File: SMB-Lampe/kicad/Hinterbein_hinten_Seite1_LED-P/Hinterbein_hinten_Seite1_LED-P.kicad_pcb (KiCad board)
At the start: 2 copper layers, 7 x 20 mm, 10 parts, among them J1 Conn_01x01_Pin, J2 Conn_01x01_Pin, J3 Conn_01x01_Pin, J4 Conn_01x01_Pin, J5 Conn_01x01_Pin, J6 Conn_01x01_Pin

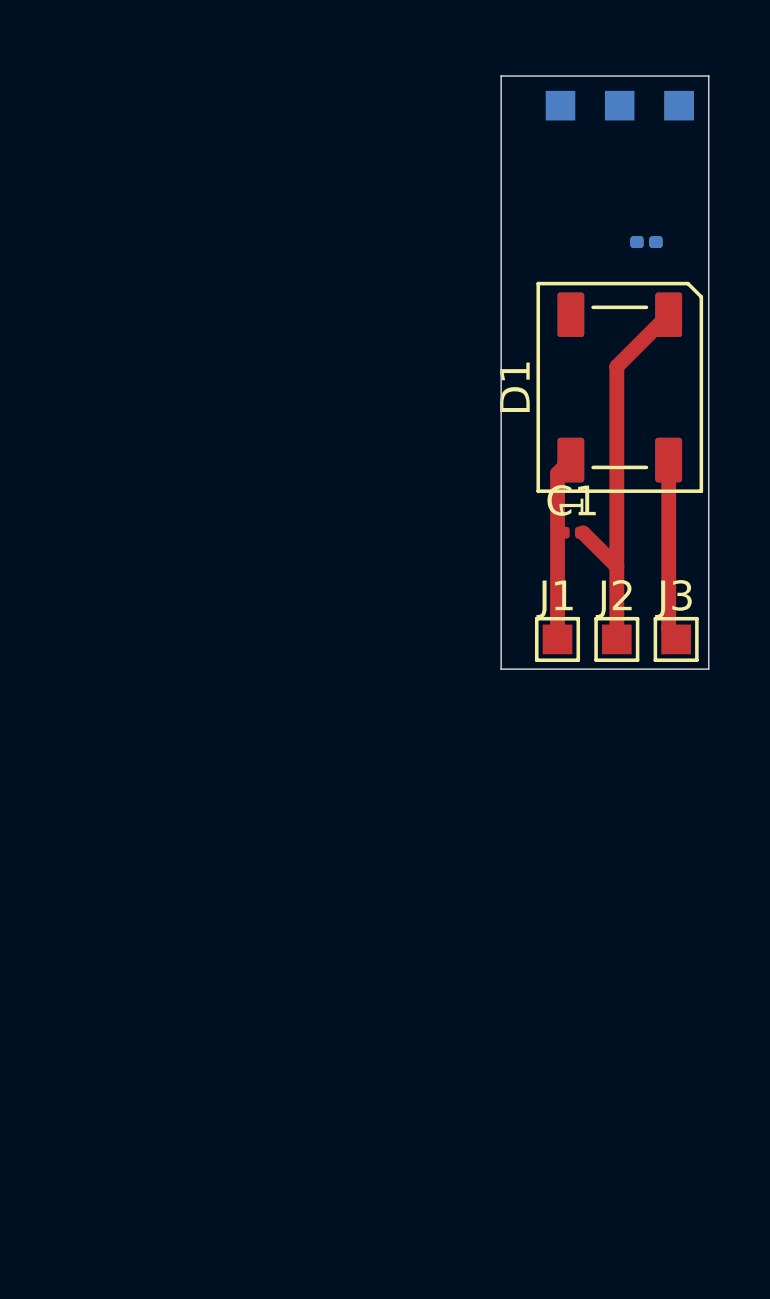
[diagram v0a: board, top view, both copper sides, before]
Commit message: Hinterbein Seite 1/2 erstellt
Anschlüsse zwischen den Platinen mit MountingHoles. Eigenes MountingHole Erstellt
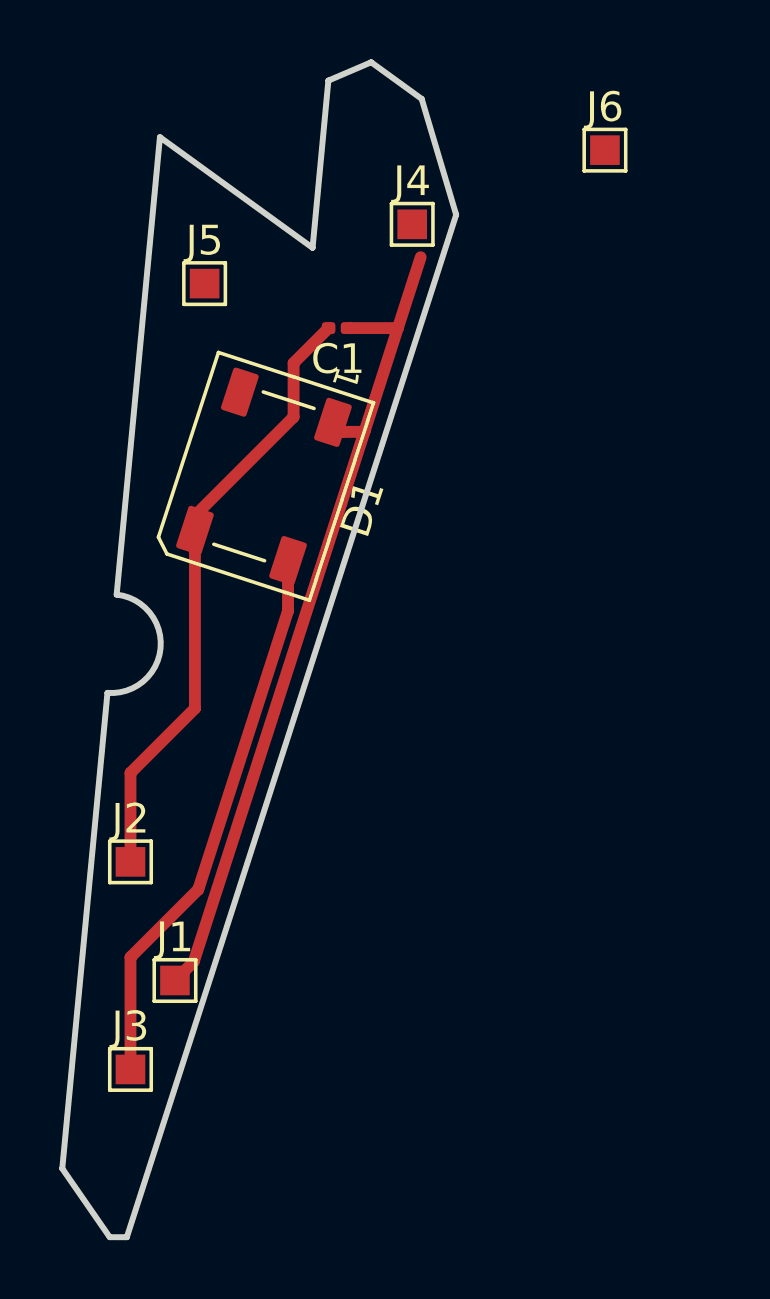
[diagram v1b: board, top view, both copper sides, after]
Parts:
- removed C2: 100nF, Capacitor_SMD:C_0201_0603Metric
- removed D2: WS2812B, LED_SMD:LED_WS2812B_PLCC4_5.0x5.0mm_P3.2mm
- J4, J5, J6: moved to F.Cu
- moved J3 23.4 mm to (127.5, 93.5)
- moved J2 18.0 mm to (127.5, 86.5)
- moved J1 17.3 mm to (129.0, 90.5)
- moved J5 15.2 mm to (130.0, 67.0), turned to 0 degrees
- moved D1 12.4 mm to (132.0, 73.5), turned to -108 degrees
- moved C1 10.5 mm to (134.5, 68.5), turned to 180 degrees
- moved J4 6.40 mm to (137.0, 65.0), turned to 0 degrees
- moved J6 2.92 mm to (143.5, 62.5), turned to 0 degrees
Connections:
- D1 pad 2: /Data_In -> /Data_OUT
- D1 pad 4: Net-(D1-DIN) -> /Data_In
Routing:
- net /+5V: track 6.24 -> 28.7 mm
- net /Data_In: track 6.15 -> 18.6 mm
- net GND: track 13.3 -> 20.8 mm
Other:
- board size 7 x 20 mm -> 13.3 x 39.6 mm
- board text added: "-108°"

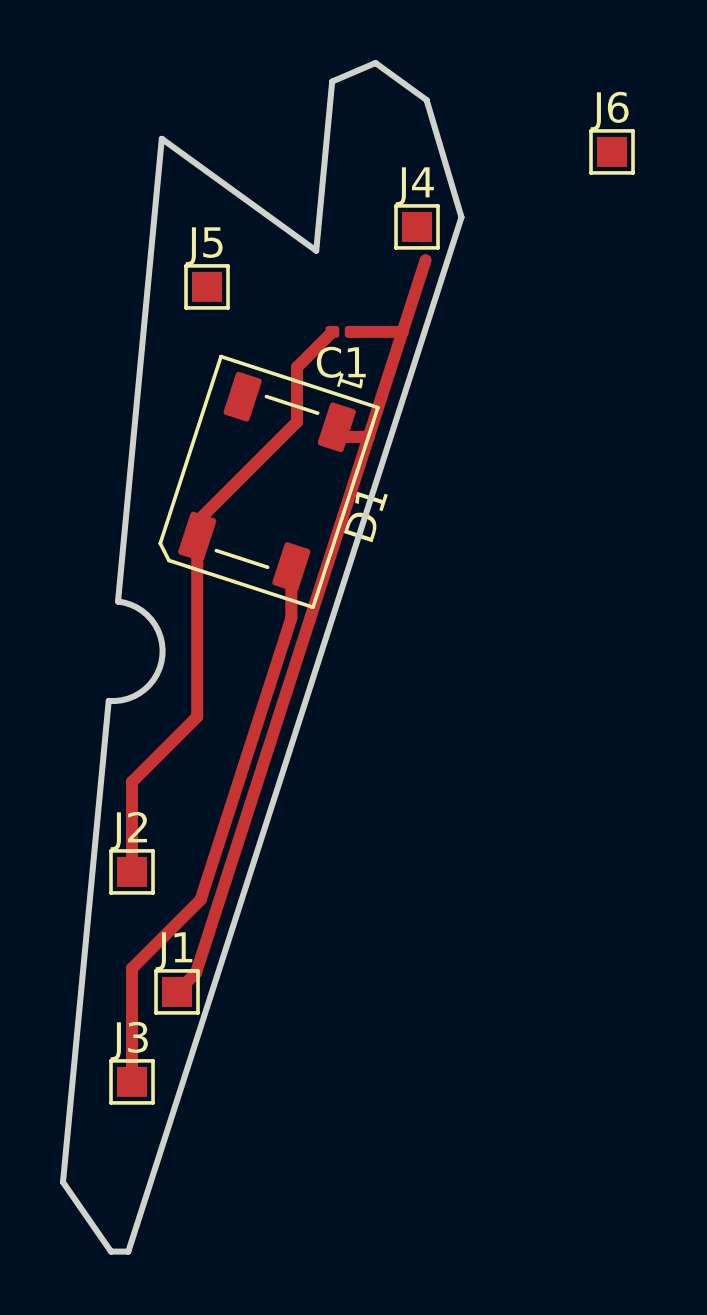
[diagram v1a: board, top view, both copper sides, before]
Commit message: Hinterbein Hinten fertig
Seite 1 und Seite 2 von Hinterbein hinten Sind fertig
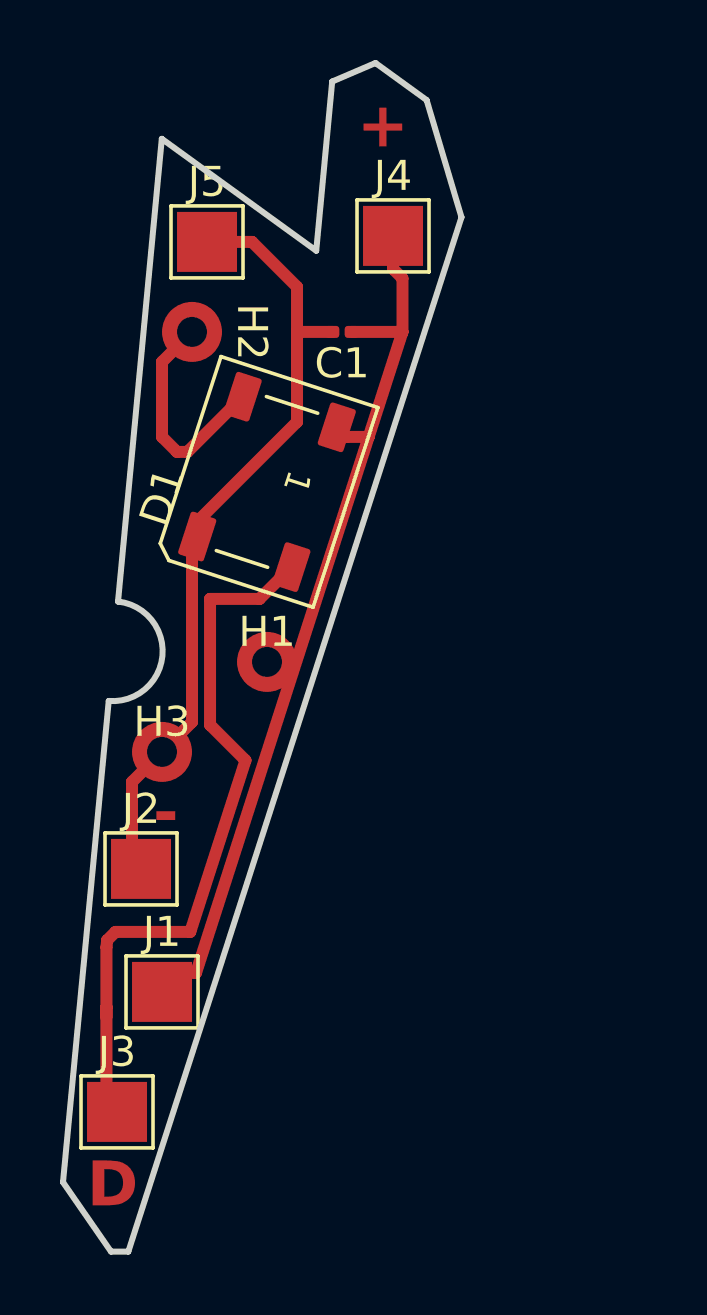
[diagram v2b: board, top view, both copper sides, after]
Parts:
- removed J6: Conn_01x01_Pin, TestPoint:TestPoint_Pad_1.0x1.0mm
- added H1: MountingHole_Pad, Eigenen_Library:MountingHole D2 x d1 test, F.Cu at (132.0, 79.5)
- added H2: MountingHole_Pad, Eigenen_Library:MountingHole D2 x d1 test, F.Cu at (129.5, 68.5)
- added H3: MountingHole_Pad, Eigenen_Library:MountingHole D2 x d1 test, F.Cu at (128.5, 82.5)
- J1, J2, J3, J4, J5: footprint TestPoint:TestPoint_Pad_1.0x1.0mm -> TestPoint:TestPoint_Pad_2.0x2.0mm
- moved J5 1.50 mm to (130.0, 65.5)
- moved J3 1.12 mm to (127.0, 94.5)
- moved J4 0.85 mm to (136.2, 65.3)
- moved J1 0.50 mm to (128.5, 90.5)
- moved J2 0.32 mm to (127.8, 86.4)
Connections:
- net /+5V renamed /+5V_IN_Hauptplatine
- net /Data_In renamed /Data_IN_Hauptplatine
- D1 pad 2: /Data_OUT -> /Data_OUT_Hinterbein_hinten_Seite2
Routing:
- net /Data_OUT_Hinterbein_hinten_Seite2: track 0.00 -> 7.57 mm
- net GND: track 20.8 -> 27.8 mm
- net /Data_IN_Hauptplatine: track 18.6 -> 24.1 mm
- net /+5V_IN_Hauptplatine: track 28.7 -> 30.1 mm
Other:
- board text added: "+"
- board text added: "-"
- board text added: "-108"
- board text added: "D"
- board text removed: "-108°"

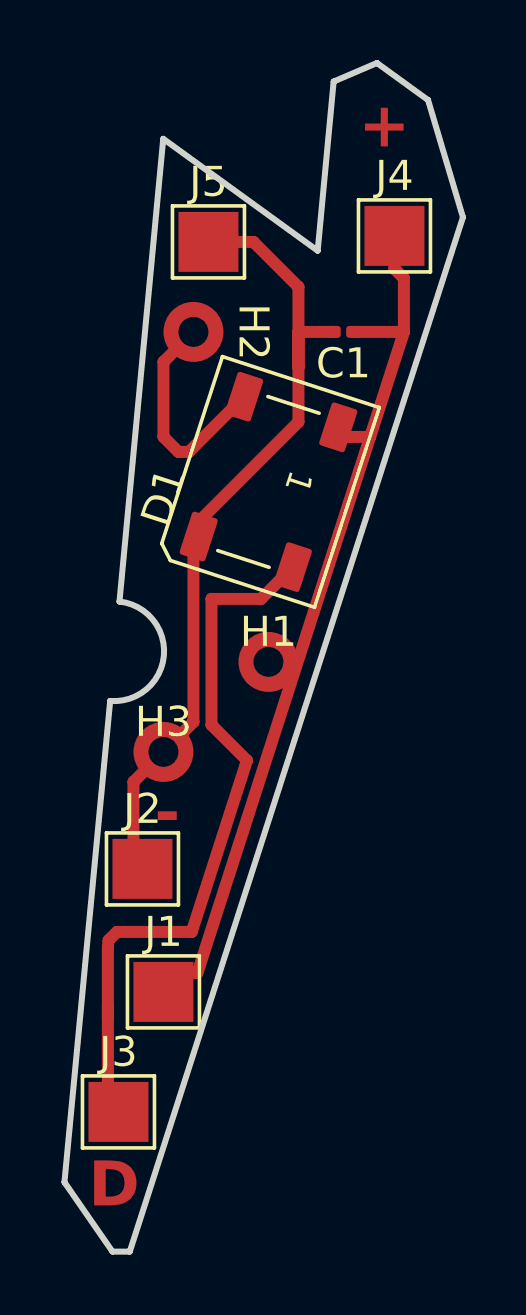
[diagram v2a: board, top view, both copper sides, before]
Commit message: Vorderes Hinterbein fertig
Alle Platinen sind fertig beschaltet
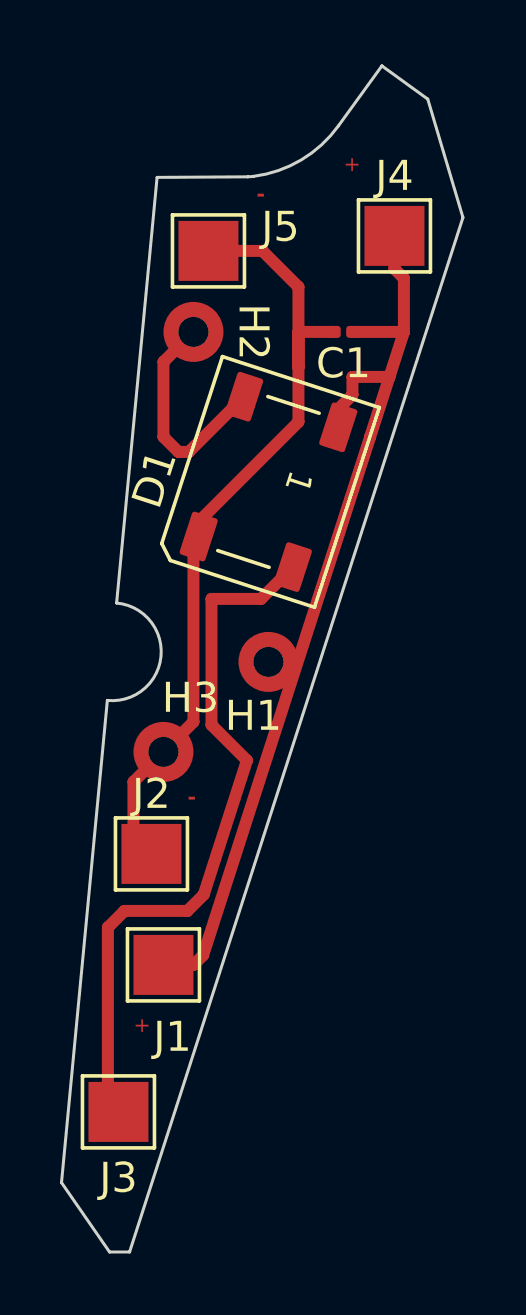
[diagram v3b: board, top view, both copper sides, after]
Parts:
- moved J1 0.90 mm to (128.5, 89.6)
- moved J2 0.58 mm to (128.1, 85.9)
- moved J5 0.30 mm to (130.0, 65.8)
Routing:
- net /+5V_IN_Hauptplatine: track 30.1 -> 31.4 mm
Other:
- board size 13.3 x 39.6 mm -> 13.4 x 39.5 mm
- board text removed: "D"

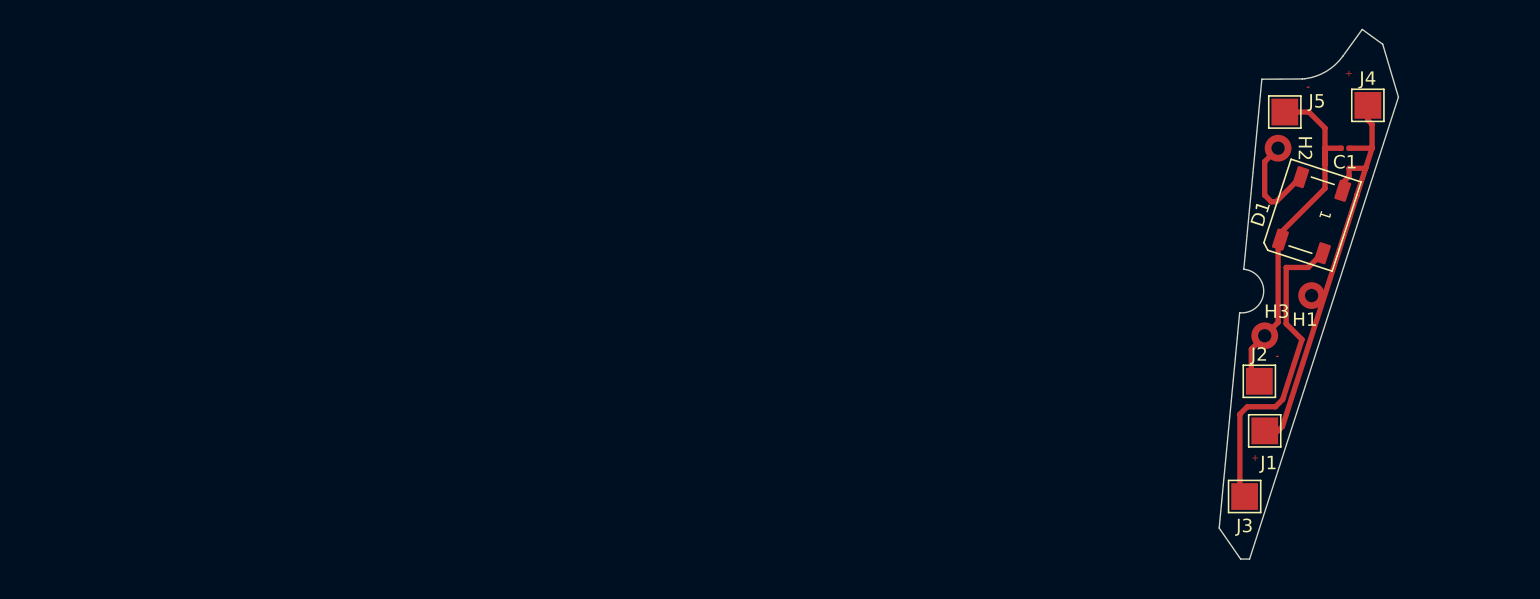
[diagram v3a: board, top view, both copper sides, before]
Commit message: Hinterbeine Geändert teilweiße Körper
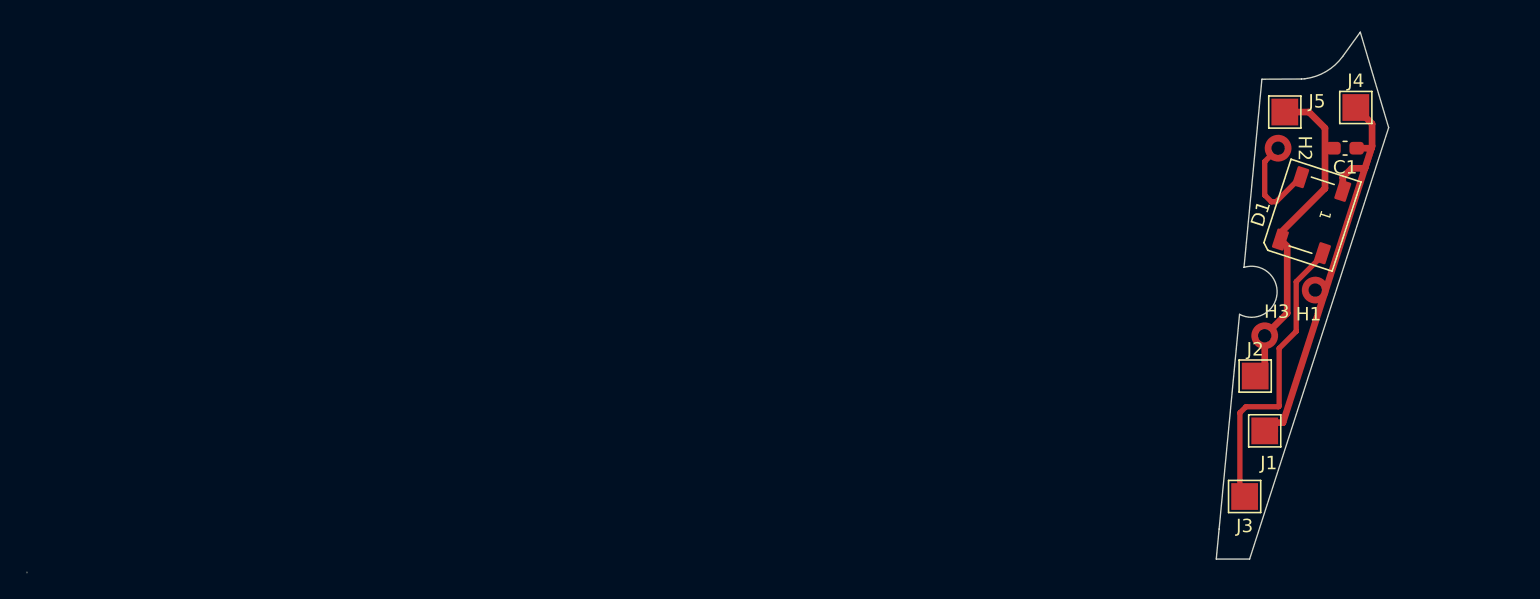
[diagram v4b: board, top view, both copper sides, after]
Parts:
- C1: footprint Capacitor_SMD:C_0201_0603Metric -> Capacitor_SMD:C_0603_1608Metric_Pad1.08x0.95mm_HandSolder
- moved J4 0.91 mm to (135.3, 65.5)
- moved J2 0.50 mm to (127.8, 85.5)
- moved H1 0.49 mm to (132.3, 79.1)
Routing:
- net GND: track 27.6 -> 31.2 mm
- net /+5V_IN_Hauptplatine: track 31.4 -> 34.8 mm
- net /Data_IN_Hauptplatine: track 23.7 -> 22.3 mm
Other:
- board size 13.4 x 39.5 mm -> 101.7 x 40.3 mm
- board text removed: "+"
- board text removed: "-"

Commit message: Alle Platinen sind fertig zur Fertigung
Aus diesem Stand folgt das erste fertig leuchtende Pferd
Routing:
- net (no net): track 0.00 -> 3.30 mm
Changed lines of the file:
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@@
+	)
+	(segment
+		(start 135 63.1)
+		(end 135 63.7)
+		(width 0.2)
+		(layer "F.Cu")
+		(net 0)
+	)
+	(segment
+		(start 127.1 83.7)
+		(end 127.5 83.7)
+		(width 0.2)
+		(layer "F.Cu")
+		(net 0)
+	)
+	(segment
+		(start 128.2 91.7)
+		(end 128.8 91.7)
+		(width 0.2)
+		(layer "F.Cu")
+		(net 0)
+	)
+	(segment
+		(start 128.5 91.4)
+		(end 128.5 92)
+		(width 0.2)
+		(layer "F.Cu")
+		(net 0)
+	)
+	(segment
+		(start 131.6 65)
+		(end 132.1 65)
+		(width 0.2)
+		(layer "F.Cu")
+		(net 0)
+	)
+	(segment
+		(start 134.7 63.4)
+		(end 135.3 63.4)
+		(width 0.2)
+		(layer "F.Cu")
+		(net 0)
 	)
 	(segment
